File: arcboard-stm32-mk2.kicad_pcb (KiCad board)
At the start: 2 copper layers, 60 x 60 mm, 74 parts, among them J1 Conn_01x04_Socket, J17 Conn_01x04_Socket, J2 Conn_01x04_Socket, J3 Conn_01x04_Socket, J4 Conn_01x04_Socket, J5 Conn_01x02_Socket, U1 XC6210B332MR-G, U13 2N7002, U14 W25Q128JVSIQTR, U15 TS-1187A-B-A-B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

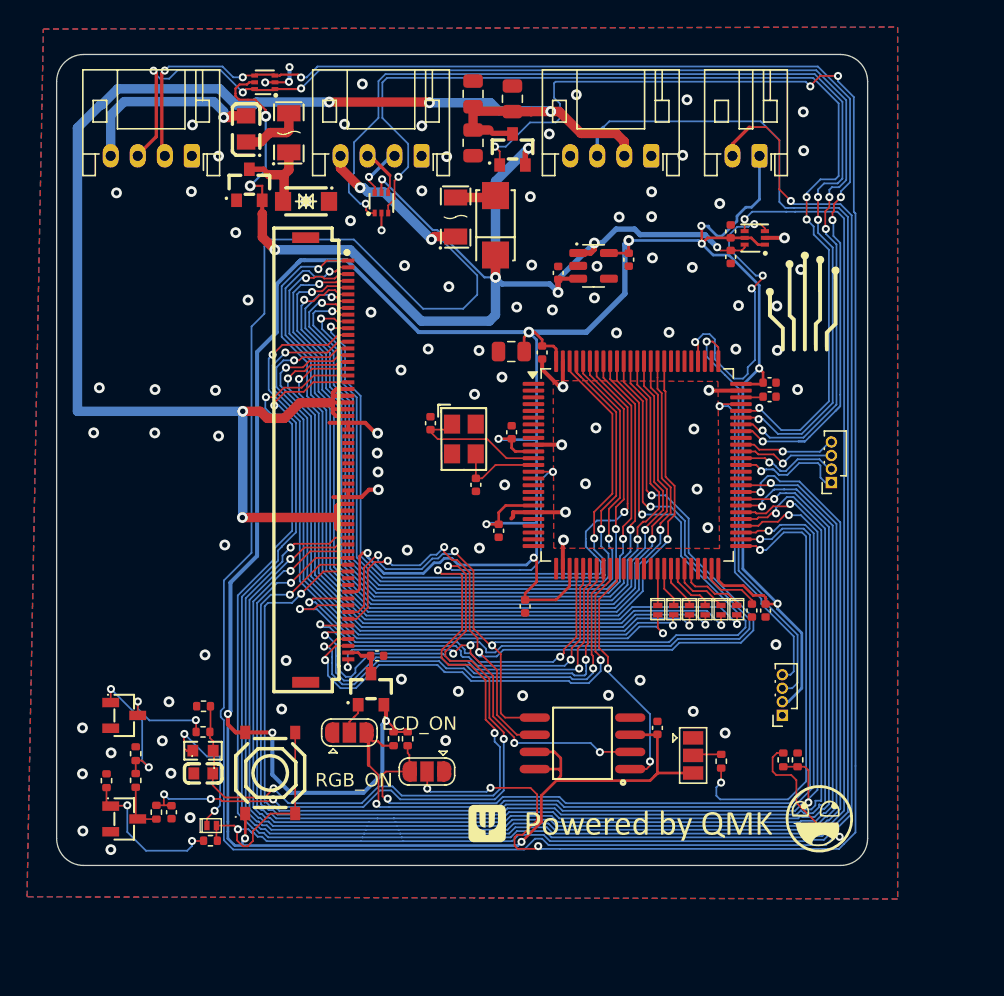
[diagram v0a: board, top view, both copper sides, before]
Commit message: starting readme, added haptic
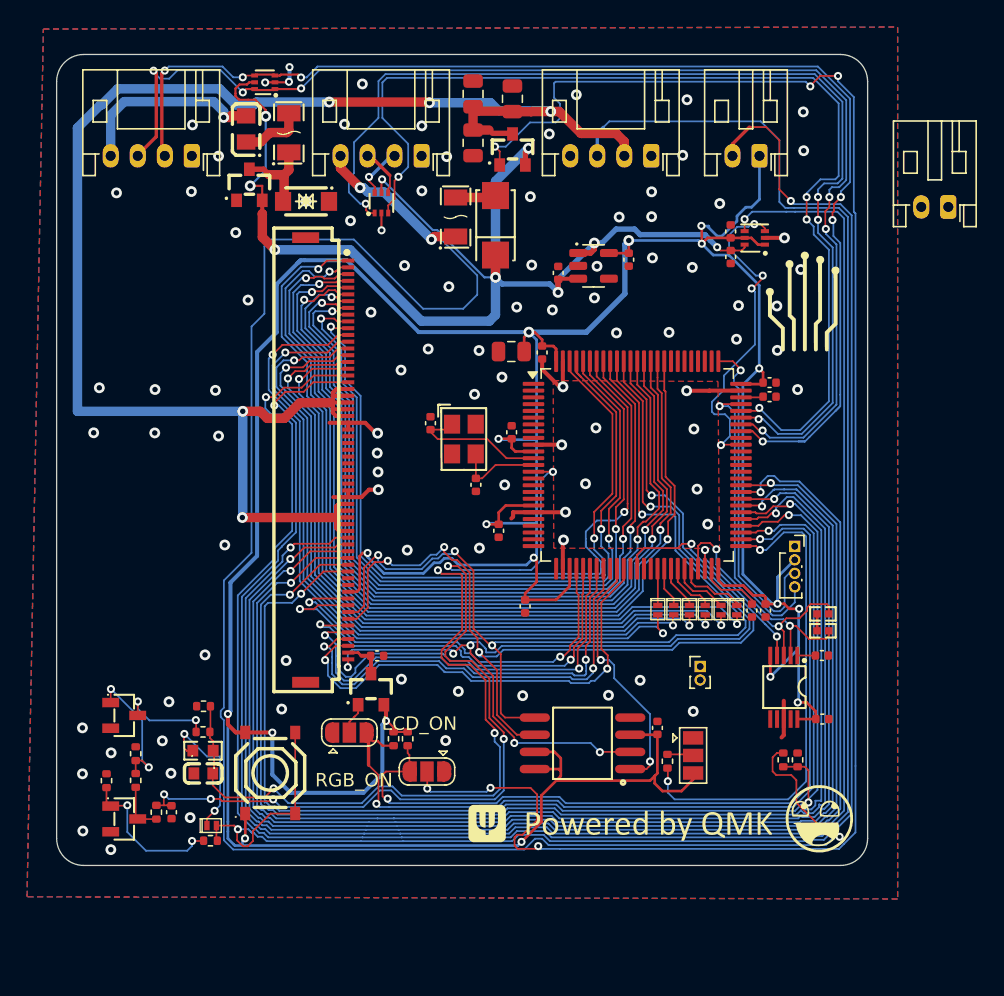
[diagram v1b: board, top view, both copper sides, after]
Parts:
- removed J4: Conn_01x04_Socket, Connector_PinSocket_1.00mm:PinSocket_1x04_P1.00mm_Vertical
- added C2: 1uF, Capacitor_SMD:C_0402_1005Metric, F.Cu at (126.6, 114.5)
- added C4: 1uF, Capacitor_SMD:C_0402_1005Metric, F.Cu at (126.7, 119.2)
- added J6: Conn_01x02_Socket, Connector_PinHeader_1.00mm:PinHeader_1x02_P1.00mm_Vertical, F.Cu at (117.6, 115.3)
- added J7: Conn_01x02_Socket, Connector_JST:JST_PH_S2B-PH-K_1x02_P2.00mm_Horizontal, F.Cu at (136.0, 81.3)
- added R13: 0402WGF2201TCE, kicad-libraries:R0402, F.Cu at (126.7, 112.6)
- added R4: 0402WGF2201TCE, kicad-libraries:R0402, F.Cu at (126.7, 111.4)
- added U5: DRV2605LDGSR, kicad-libraries:VSSOP-10_L3.0-W3.0-P0.50-LS4.9-BL, F.Cu at (123.8, 116.8)
- moved J2 12.5 mm to (124.6, 106.4), turned to 0 degrees
- moved R12 3.98 mm to (115.2, 122.3)
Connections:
- U2 pad 34: LCD_BL -> unconnected-(U2-PC5-Pad34)
- U2 pad 36: unconnected-(U2-PB1-Pad36) -> LCD_BL
- U2 pad 38: unconnected-(U2-PE7-Pad38) -> HAPTIC_PWM
- U2 pad 47: unconnected-(U2-PB10-Pad47) -> I2C_SCL
- U2 pad 48: unconnected-(U2-PB11-Pad48) -> I2C_SDA
- U2 pad 63: SPARE1 -> unconnected-(U2-PC6-Pad63)
- U2 pad 64: SPARE2 -> unconnected-(U2-PC7-Pad64)
- U2 pad 65: SPARE3 -> unconnected-(U2-PC8-Pad65)
- U2 pad 66: SPARE4 -> LED_SIG_OUTPUT
- U2 pad 79: LED_SIG_OUTPUT -> unconnected-(U2-PC11-Pad79)
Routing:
- net I2C_SCL: track 0.00 -> 17.7 mm, vias 0 -> 2
- net I2C_SDA: track 0.00 -> 17.0 mm, vias 0 -> 2
- net HAPTIC_PWM: track 0.00 -> 16.3 mm, vias 0 -> 2
- net +3V3: track 288.6 -> 303.4 mm, vias 15 -> 18
- net SPARE1: track 8.63 -> 0.00 mm, vias 1 -> 0
- net SPARE2: track 7.74 -> 0.00 mm, vias 1 -> 0
- net SPARE3: track 7.30 -> 0.00 mm, vias 1 -> 0
- net SPARE4: track 7.20 -> 0.00 mm, vias 1 -> 0
- net SWCLK: track 31.4 -> 25.2 mm
- net GND: track 29.8 -> 34.2 mm, vias 97 -> 95
- net SPLIT_HAND: track 33.2 -> 36.5 mm
- net SWDIO: track 24.9 -> 22.3 mm
- net Net-(U5-REG): track 0.00 -> 1.34 mm
- net LED_SIG_OUTPUT: track 23.6 -> 24.8 mm
- net LCD_BL: track 33.9 -> 34.6 mm

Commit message: finishing haptic bits
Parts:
- moved LOGO3 46.0 mm to (81.2, 100.7), turned to 90 degrees
- moved J7 14.7 mm to (121.6, 84.2), turned to 90 degrees
- moved C18 6.85 mm to (117.7, 76.6)
- moved C19 6.85 mm to (117.7, 78.5)
- moved LED-LVL1 6.42 mm to (119.7, 77.4)
- moved J5 3.90 mm to (125.9, 77.5)
- moved J6 1.18 mm to (117.6, 116.5), turned to 180 degrees
- moved R4 0.31 mm to (126.4, 111.4)
- moved R13 0.30 mm to (126.4, 112.7)
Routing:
- net +3V3: track 303.4 -> 359.1 mm, vias 18 -> 22
- net HAPTIC_pos: track 0.00 -> 48.6 mm, vias 0 -> 2
- net HAPTIC_neg: track 0.00 -> 46.9 mm, vias 0 -> 1
- net LED_SIG_OUTPUT: track 24.8 -> 43.4 mm, vias 4 -> 2
- net +5V: track 91.3 -> 102.8 mm
- net I2C_SDA: track 17.0 -> 26.5 mm, vias 2 -> 4
- net I2C_SCL: track 17.7 -> 25.3 mm
- net GND: track 34.2 -> 40.6 mm, vias 95 -> 93
- net Net-(D11-A): track 121.9 -> 115.7 mm, vias 2 -> 1
- net LED_KEYS_DI: track 137.7 -> 143.4 mm
- net LED_EXT_DI: track 157.8 -> 163.1 mm, vias 1 -> 3
- net USB_DP: track 78.5 -> 79.6 mm
- net USB_DM: track 79.9 -> 81.0 mm
- net SERIAL_CONN_RX: track 93.4 -> 94.5 mm
- net RGB_5V: track 123.7 -> 122.6 mm
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
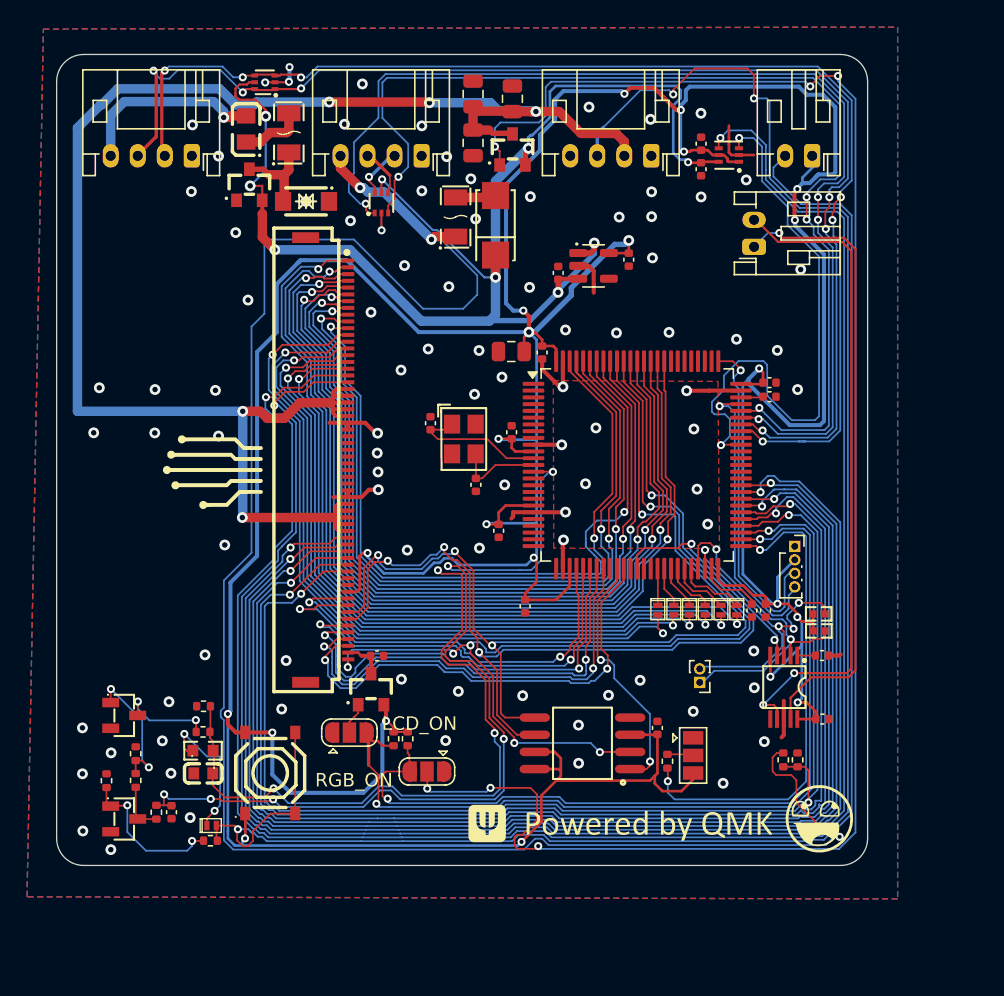
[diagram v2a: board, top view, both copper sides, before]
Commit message: adding dac amp
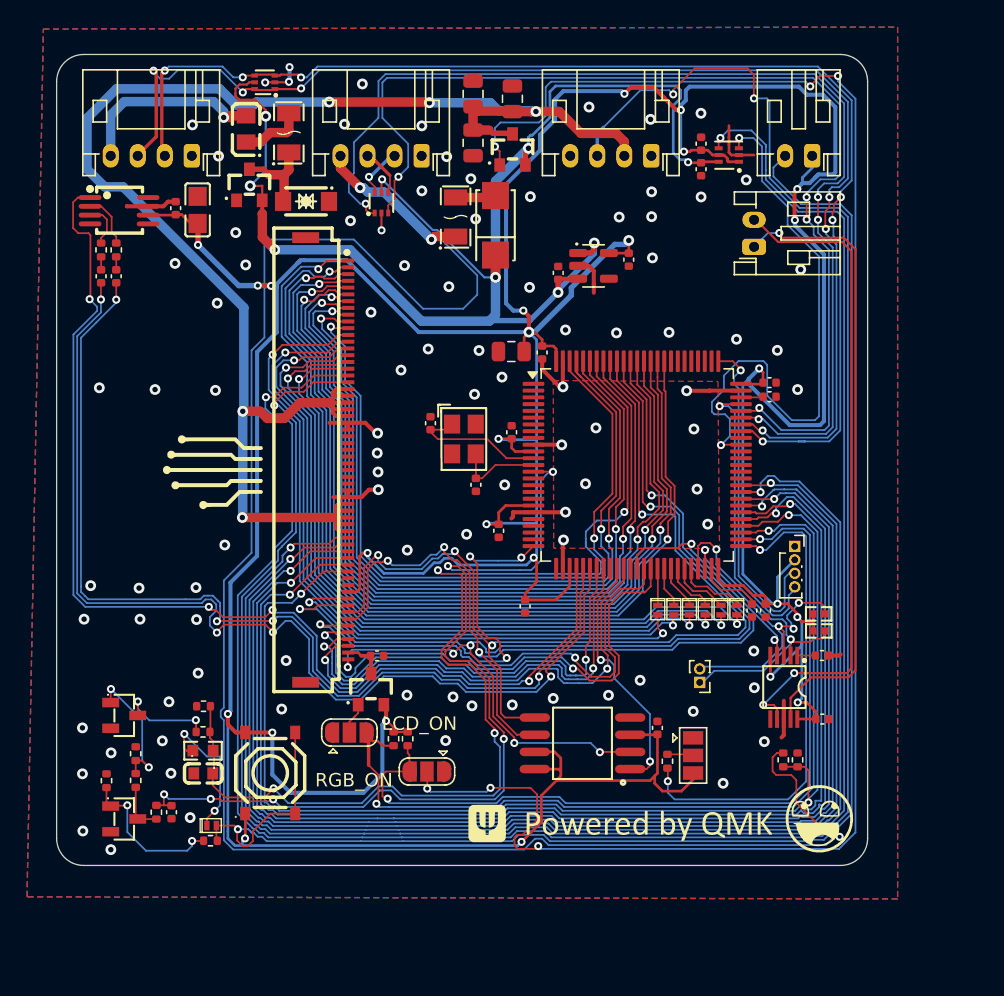
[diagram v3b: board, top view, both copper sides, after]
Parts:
- added C24: 1uF, Capacitor_SMD:C_0402_1005Metric, F.Cu at (78.8, 81.4)
- added C25: GCM21BR70J106KE22L, kicad-libraries:C0805, F.Cu at (80.4, 81.5)
- added C26: 100nF, Capacitor_SMD:C_0402_1005Metric, F.Cu at (74.4, 86.4)
- added C28: 100nF, Capacitor_SMD:C_0402_1005Metric, F.Cu at (73.3, 86.4)
- added R17: 10k, Resistor_SMD:R_0402_1005Metric, F.Cu at (73.3, 84.5)
- added R5: 10k, Resistor_SMD:R_0402_1005Metric, F.Cu at (74.4, 84.5)
- added U6: PAM8302AASCR, kicad-libraries:MSOP-8_L3.0-W3.0-P0.65-LS5.0-BL, F.Cu at (74.6, 81.6)
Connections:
- U2 pad 25: unconnected-(U2-PA2-Pad25) -> PMW_MOTION
- U2 pad 29: PMW_MOTION -> AMP_SD
- U2 pad 30: PMW_CS -> AMP_IN-
- U2 pad 31: LCD_RST -> AMP_IN+
- U2 pad 39: unconnected-(U2-PE8-Pad39) -> PMW_CS
- U2 pad 40: unconnected-(U2-PE9-Pad40) -> LCD_RST
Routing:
- net AMP_SD: track 0.00 -> 82.2 mm, vias 0 -> 4
- net AMP_IN+: track 0.00 -> 77.7 mm, vias 0 -> 4
- net AMP_IN-: track 0.00 -> 75.4 mm, vias 0 -> 4
- net +3V3: track 359.1 -> 371.8 mm, vias 22 -> 25
- net PMW_CS: track 33.0 -> 40.2 mm
- net RGB_5V: track 122.6 -> 115.7 mm
- net LCD_RST: track 33.7 -> 40.3 mm
- net Net-(U6-IN-): track 0.00 -> 4.00 mm
- net GND: track 40.6 -> 44.3 mm, vias 93 -> 97
- net Net-(U6-IN+): track 0.00 -> 3.30 mm
- net PMW_MOTION: track 31.0 -> 33.9 mm, vias 2 -> 4
- net LCD_DC: track 33.2 -> 34.3 mm
- net LCD_CS: track 33.6 -> 34.6 mm
- net LCD_BL: track 34.6 -> 35.6 mm
- net Net-(C28-Pad1): track 0.00 -> 0.96 mm
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
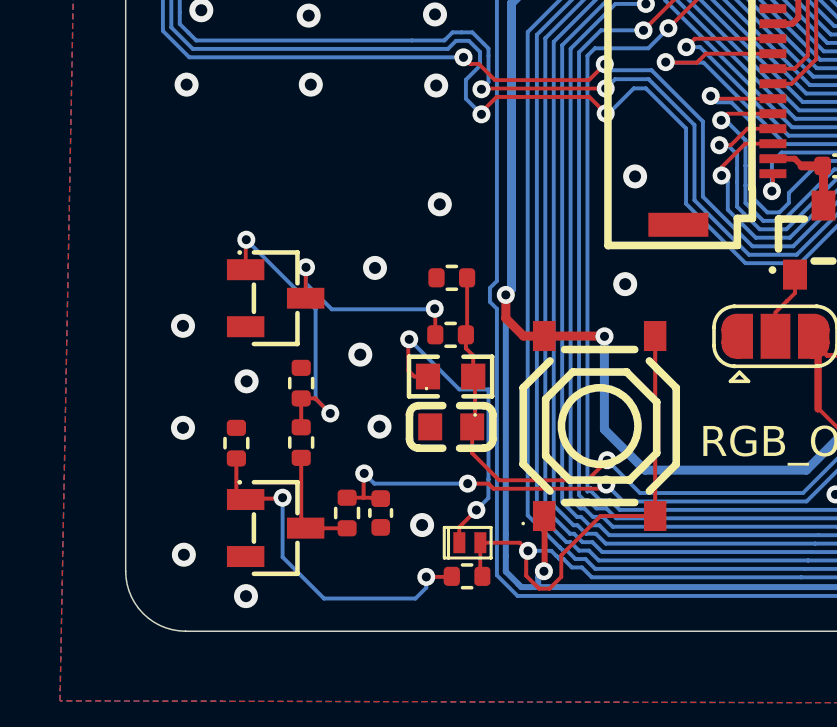
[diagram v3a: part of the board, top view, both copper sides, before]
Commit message: adding piezo that does not fit
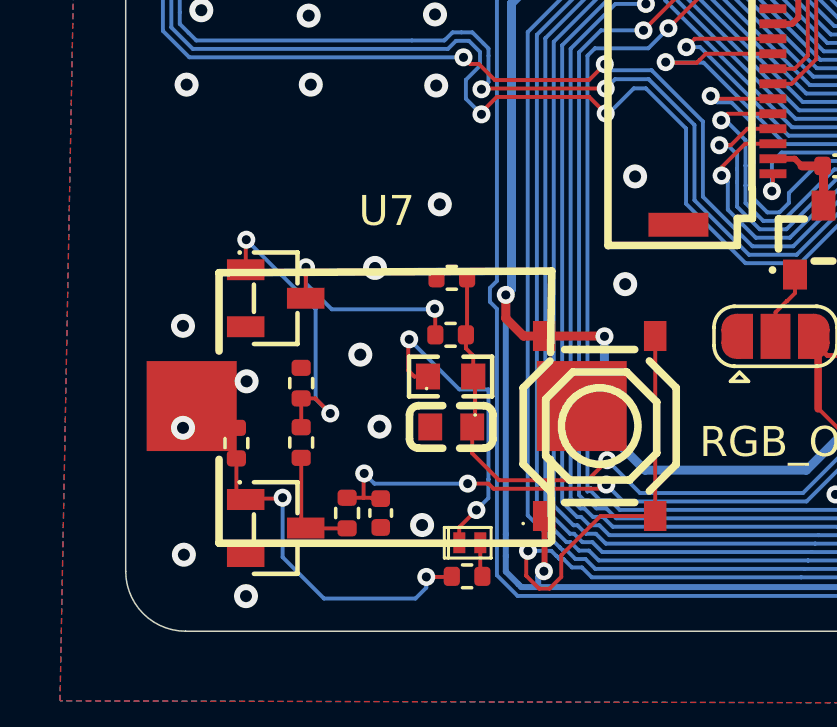
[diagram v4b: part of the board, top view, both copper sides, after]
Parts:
- added U7: AST1109MLQ, kicad-libraries:BUZ-SMD_L11.0-W9.0, F.Cu at (78.7, 122.5)
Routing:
- net VO-: vias 0 -> 2
- net GND: vias 97 -> 95
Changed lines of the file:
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@@
 		)
 	)
+	(footprint "kicad-libraries:BUZ-SMD_L11.0-W9.0"
+		(layer "F.Cu")
+		(at 78.7 122.493996)
+		(descr "BUZ-SMD_L11.0-W9.0 footprint")
+		(tags "BUZ-SMD_L11.0-W9.0 footprint C9900020429")
+		(property "Reference" "U7"
+			(at 0 -6.5 0)
+			(layer "F.SilkS")
+			(effects
+				(font
+					(size 1 1)
+					(thickness 0.15)
+				)
+			)
+		)
+		(property "Value" "AST1109MLQ"
+			(at 0 6.572009 0)
+			(layer "F.Fab")
+			(effects
+				(font
+					(size 1 1)
+					(thickness 0.15)
+				)
+			)
+		)
+		(property "Datasheet" "https://item.szlcsc.com/1056289.html"
+			(at 0 0 0)
+			(layer "F.Fab")
+			(hide yes)
+			(effects
+				(font
+					(size 1.27 1.27)
+					(thickness 0.15)
+				)
+			)
+		)
+		(property "Description" ""
+			(at 0 0 0)
+			(layer "F.Fab")
+			(hide yes)
+			(effects
+				(font
+					(size 1.27 1.27)
+					(thickness 0.15)
+				)
+			)
+		)
+		(property "LCSC" "C9900020429"
+			(at 0 0 0)
+			(unlocked yes)
+			(layer "F.Fab")
+			(hide yes)
+			(effects
+				(font
+					(size 1 1)
+					(thickness 0.15)
+				)
+			)
+		)
+		(sheetname "/")
+		(sheetfile "arcboard-stm32-mk2.kicad_sch")
+		(attr smd)
+		(fp_line
+			(start -5.588011 -4.445009)
+			(end -5.588011 -1.834163)
+			(stroke
+				(width 0.254001)
+				(type solid)
+			)
+			(layer "F.SilkS")
+		)
+		(fp_line
+			(start -5.588011 -4.445009)
+			(end 5.5 -4.5)
+			(stroke
+				(width 0.254001)
+				(type solid)
+			)
+			(layer "F.SilkS")
+		)
+		(fp_line
+			(start -5.588011 1.778004)
+			(end -5.588011 4.572009)
+			(stroke
+				(width 0.254001)
+				(type solid)
+			)
+			(layer "F.SilkS")
+		)
+		(fp_line
+			(start -5.588011 4.572009)
+			(end 5.411989 4.572009)
+			(stroke
+				(width 0.254001)
+				(type solid)
+			)
+			(layer "F.SilkS")
+		)
+		(fp_line
+			(start 5.461011 1.778004)
+			(end 5.5 4.5)
+			(stroke
+				(width 0.254001)
+				(type solid)
+			)
+			(layer "F.SilkS")
+		)
+		(fp_line
+			(start 5.5 -4.5)
+			(end 5.461011 -1.778004)
+			(stroke
+				(width 0.254001)
+				(type solid)
+			)
+			(layer "F.SilkS")
+		)
+		(fp_circle
+			(center -7.490119 4.5)
+			(end -7.460122 4.5)
+			(stroke
+				(width 0.059995)
+				(type solid)
+			)
+			(fill no)
+			(layer "Rescue")
+		)
+		(fp_poly
+			(pts
+				(xy -5.500025 4.5) (xy -5.500025 -4.500025) (xy 5.5 -4.500025) (xy 5.5 4.5)
+			)
+			(stroke
+				(width 0.15)
+				(type solid)
+			)
+			(fill yes)
+			(layer "Rescue")
+		)
+		(fp_poly
+			(pts
+				(xy -5.490119 -1) (xy -5.490119 1) (xy -7.490119 1) (xy -7.490119 -1)
+			)
+			(stroke
+				(width 0.15)
+				(type solid)
+			)
+			(fill yes)
+			(layer "Rescue")
+		)
+		(fp_poly
+			(pts
+				(xy 7.490119 -1) (xy 7.490119 1) (xy 5.490119 1) (xy 5.490119 -1)
+			)
+			(stroke
+				(width 0.15)
+				(type solid)
+			)
+			(fill yes)
+			(layer "Rescue")
+		)
+		(fp_text user "${REFERENCE}"
+			(at 0 0.036005 0)
+			(layer "F.Fab")
+			(effects
+				(font
+					(size 1 1)
+					(thickness 0.15)
+				)
+			)
+		)
+		(pad "1" smd rect
+			(at -6.500127 0 90)
+			(size 3 3)
+			(layers "F.Cu" "F.Mask" "F.Paste")
+			(net 132 "VO-")
+			(pinfunction "1")
+			(pintype "unspecified")
+		)
+		(pad "2" smd rect
+			(at 6.500127 0 90)
+			(size 3 3)
+			(layers "F.Cu" "F.Mask" "F.Paste")
+			(net 130 "VO+")
+			(pinfunction "2")
+			(pintype "unspecified")
+		)
+		(embedded_fonts no)
+		(model "packages3d/BUZ-SMD_L11.0-W9.0.step"
+			(offset
+				(xyz 0 0 0)
+			)
+			(scale
+				(xyz 1 1 1)
+			)
+			(rotate
+				(xyz 0 0 0)
+			)
+		)
+	)
 	(footprint "kicad-libraries:cyboard-logo-10mm"
 		(layer "F.Cu")
@@
 	)
 	(via
-		(at 71.91 123.22)
-		(size 0.8)
-		(drill 0.4)
-		(layers "F.Cu" "B.Cu")
-		(net 1)
-	)
-	(via
-		(at 74.03 121.67)
-		(size 0.8)
-		(drill 0.4)
-		(layers "F.Cu" "B.Cu")
-		(net 1)
-	)
-	(via
 		(at 78.31 117.89)
 		(size 0.8)
@@
 		(net 131)
 	)
+	(via
+		(at 71.91 123.22)
+		(size 0.8)
+		(drill 0.4)
+		(layers "F.Cu" "B.Cu")
+		(net 132)
+	)
+	(via
+		(at 74.03 121.67)
+		(size 0.8)
+		(drill 0.4)
+		(layers "F.Cu" "B.Cu")
+		(net 132)
+	)
 	(zone
